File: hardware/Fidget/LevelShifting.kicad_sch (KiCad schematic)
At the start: 20 parts

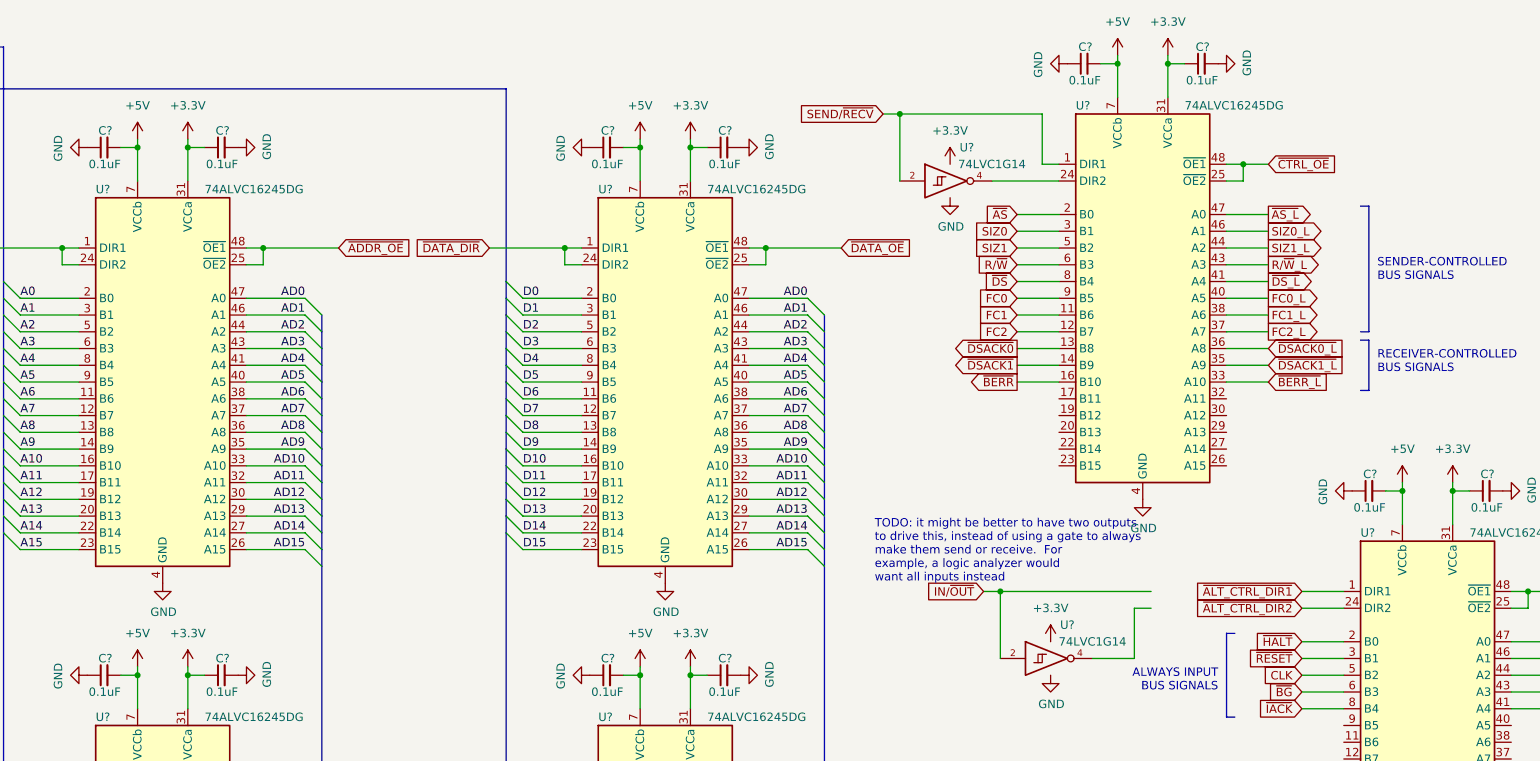
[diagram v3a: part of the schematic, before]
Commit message: Added jumper to select bus voltage
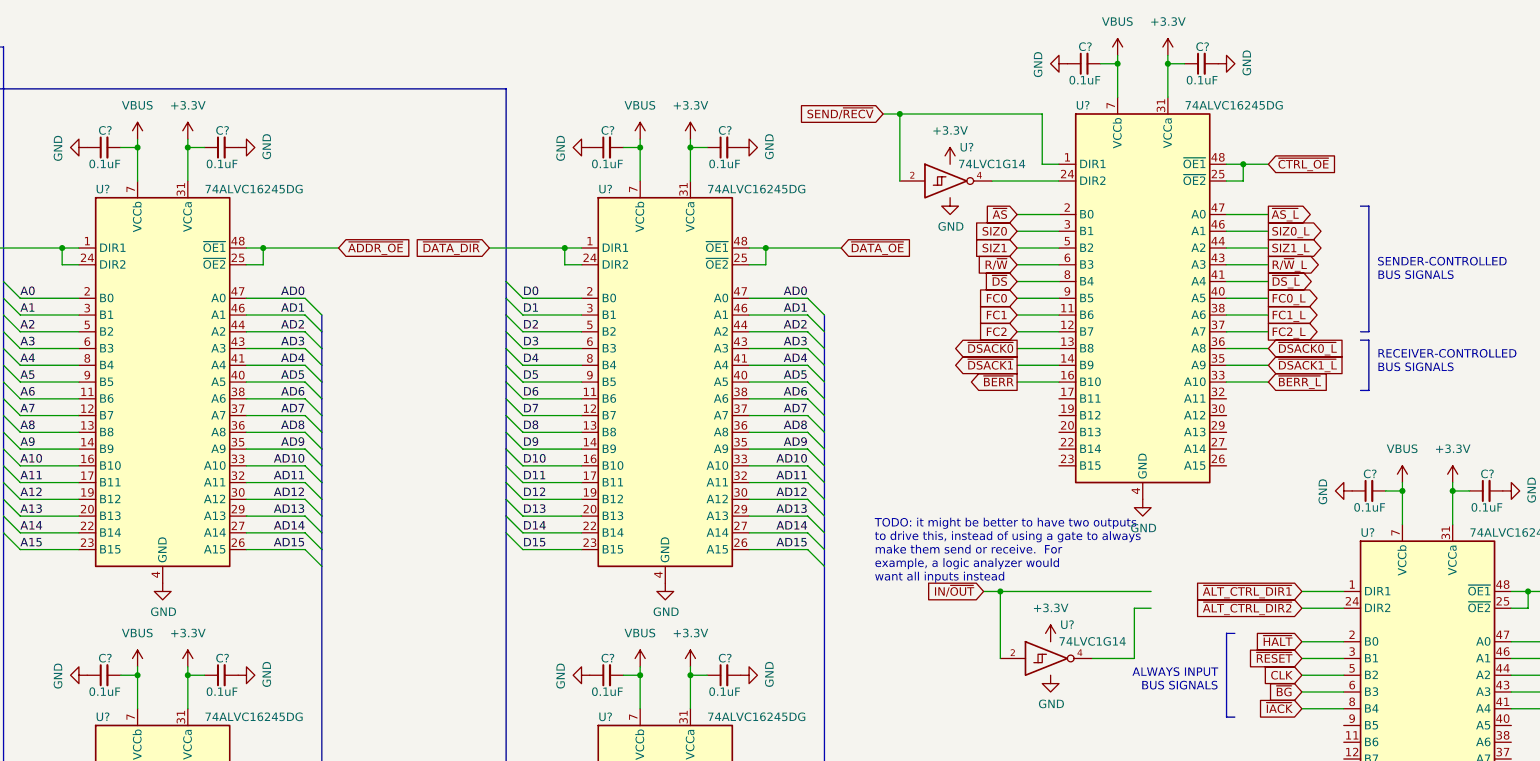
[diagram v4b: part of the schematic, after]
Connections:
- net +5V renamed VBUS
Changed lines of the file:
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@@
+    (pin "1")
+  )
+  (symbol (lib_id "power:VBUS") (at 54.61 114.3 0) (unit 1)
+    (in_bom yes) (on_board yes) (fields_autoplaced)
+    (property "Reference" "#PWR?" (id 0) (at 54.61 118.11 0)
+      (effects (font (size 1.27 1.27)) hide)
+    )
+    (property "Value" "VBUS" (id 1) (at 54.61 109.22 0))
+    (property "Footprint" "" (id 2) (at 54.61 114.3 0)
+      (effects (font (size 1.27 1.27)) hide)
+    )
+    (property "Datasheet" "" (id 3) (at 54.61 114.3 0)
+      (effects (font (size 1.27 1.27)) hide)
+    )
+    (pin "1")
+  )
+  (symbol (lib_id "power:VBUS") (at 203.2 21.59 0) (unit 1)
+    (in_bom yes) (on_board yes) (fields_autoplaced)
+    (property "Reference" "#PWR?" (id 0) (at 203.2 25.4 0)
+      (effects (font (size 1.27 1.27)) hide)
+    )
+    (property "Value" "VBUS" (id 1) (at 203.2 16.51 0))
+    (property "Footprint" "" (id 2) (at 203.2 21.59 0)
+      (effects (font (size 1.27 1.27)) hide)
+    )
+    (property "Datasheet" "" (id 3) (at 203.2 21.59 0)
+      (effects (font (size 1.27 1.27)) hide)
+    )
     (pin "1")
   )
@@
     (pin "1")
     (pin "2")
+  )
+  (symbol (lib_id "power:VBUS") (at 246.38 86.36 0) (unit 1)
+    (in_bom yes) (on_board yes) (fields_autoplaced)
+    (property "Reference" "#PWR?" (id 0) (at 246.38 90.17 0)
+      (effects (font (size 1.27 1.27)) hide)
+    )
+    (property "Value" "VBUS" (id 1) (at 246.38 81.28 0))
+    (property "Footprint" "" (id 2) (at 246.38 86.36 0)
+      (effects (font (size 1.27 1.27)) hide)
+    )
+    (property "Datasheet" "" (id 3) (at 246.38 86.36 0)
+      (effects (font (size 1.27 1.27)) hide)
+    )
+    (pin "1")
   )
   (symbol (lib_id "power:GND") (at 261.62 87.63 90) (unit 1)
@@
     (pin "1")
   )
-  (symbol (lib_id "power:+5V") (at 246.38 86.36 0) (unit 1)
-    (in_bom yes) (on_board yes) (fields_autoplaced)
-    (property "Reference" "#PWR?" (id 0) (at 246.38 90.17 0)
-      (effects (font (size 1.27 1.27)) hide)
-    )
-    (property "Value" "+5V" (id 1) (at 246.38 81.28 0))
-    (property "Footprint" "" (id 2) (at 246.38 86.36 0)
-      (effects (font (size 1.27 1.27)) hide)
-    )
-    (property "Datasheet" "" (id 3) (at 246.38 86.36 0)
-      (effects (font (size 1.27 1.27)) hide)
-    )
-    (pin "1")
-  )
   (symbol (lib_id "power:+3.3V") (at 210.82 21.59 0) (unit 1)
     (in_bom yes) (on_board yes) (fields_autoplaced)
@@
     )
     (property "Datasheet" "" (id 3) (at 254 86.36 0)
-      (effects (font (size 1.27 1.27)) hide)
-    )
-    (pin "1")
-  )
-  (symbol (lib_id "power:+5V") (at 54.61 114.3 0) (unit 1)
-    (in_bom yes) (on_board yes) (fields_autoplaced)
-    (property "Reference" "#PWR?" (id 0) (at 54.61 118.11 0)
-      (effects (font (size 1.27 1.27)) hide)
-    )
-    (property "Value" "+5V" (id 1) (at 54.61 109.22 0))
-    (property "Footprint" "" (id 2) (at 54.61 114.3 0)
-      (effects (font (size 1.27 1.27)) hide)
-    )
-    (property "Datasheet" "" (id 3) (at 54.61 114.3 0)
       (effects (font (size 1.27 1.27)) hide)
     )
@@
     (pin "5")
   )
+  (symbol (lib_id "power:VBUS") (at 130.81 114.3 0) (unit 1)
+    (in_bom yes) (on_board yes) (fields_autoplaced)
+    (property "Reference" "#PWR?" (id 0) (at 130.81 118.11 0)
+      (effects (font (size 1.27 1.27)) hide)
+    )
+    (property "Value" "VBUS" (id 1) (at 130.81 109.22 0))
+    (property "Footprint" "" (id 2) (at 130.81 114.3 0)
+      (effects (font (size 1.27 1.27)) hide)
+    )
+    (property "Datasheet" "" (id 3) (at 130.81 114.3 0)
+      (effects (font (size 1.27 1.27)) hide)
+    )
+    (pin "1")
+  )
   (symbol (lib_id "power:GND") (at 218.44 22.86 90) (unit 1)
     (in_bom yes) (on_board yes)
@@
     (pin "1")
   )
-  (symbol (lib_id "power:+5V") (at 130.81 114.3 0) (unit 1)
-    (in_bom yes) (on_board yes) (fields_autoplaced)
-    (property "Reference" "#PWR?" (id 0) (at 130.81 118.11 0)
-      (effects (font (size 1.27 1.27)) hide)
-    )
-    (property "Value" "+5V" (id 1) (at 130.81 109.22 0))
-    (property "Footprint" "" (id 2) (at 130.81 114.3 0)
-      (effects (font (size 1.27 1.27)) hide)
-    )
-    (property "Datasheet" "" (id 3) (at 130.81 114.3 0)
-      (effects (font (size 1.27 1.27)) hide)
-    )
-    (pin "1")
-  )
-  (symbol (lib_id "power:+5V") (at 54.61 34.29 0) (unit 1)
-    (in_bom yes) (on_board yes) (fields_autoplaced)
-    (property "Reference" "#PWR0136" (id 0) (at 54.61 38.1 0)
-      (effects (font (size 1.27 1.27)) hide)
-    )
-    (property "Value" "+5V" (id 1) (at 54.61 29.21 0))
-    (property "Footprint" "" (id 2) (at 54.61 34.29 0)
-      (effects (font (size 1.27 1.27)) hide)
-    )
-    (property "Datasheet" "" (id 3) (at 54.61 34.29 0)
-      (effects (font (size 1.27 1.27)) hide)
-    )
-    (pin "1")
-  )
   (symbol (lib_id "power:GND") (at 58.42 181.61 0) (unit 1)
     (in_bom yes) (on_board yes)
@@
     (pin "9")
   )
-  (symbol (lib_id "power:+5V") (at 130.81 34.29 0) (unit 1)
-    (in_bom yes) (on_board yes) (fields_autoplaced)
-    (property "Reference" "#PWR?" (id 0) (at 130.81 38.1 0)
-      (effects (font (size 1.27 1.27)) hide)
-    )
-    (property "Value" "+5V" (id 1) (at 130.81 29.21 0))
-    (property "Footprint" "" (id 2) (at 130.81 34.29 0)
-      (effects (font (size 1.27 1.27)) hide)
-    )
-    (property "Datasheet" "" (id 3) (at 130.81 34.29 0)
+  (symbol (lib_id "power:VBUS") (at 54.61 34.29 0) (unit 1)
+    (in_bom yes) (on_board yes) (fields_autoplaced)
+    (property "Reference" "#PWR?" (id 0) (at 54.61 38.1 0)
+      (effects (font (size 1.27 1.27)) hide)
+    )
+    (property "Value" "VBUS" (id 1) (at 54.61 29.21 0))
+    (property "Footprint" "" (id 2) (at 54.61 34.29 0)
+      (effects (font (size 1.27 1.27)) hide)
+    )
+    (property "Datasheet" "" (id 3) (at 54.61 34.29 0)
       (effects (font (size 1.27 1.27)) hide)
     )
@@
     (pin "9")
   )
-  (symbol (lib_id "power:+5V") (at 203.2 21.59 0) (unit 1)
-    (in_bom yes) (on_board yes) (fields_autoplaced)
-    (property "Reference" "#PWR?" (id 0) (at 203.2 25.4 0)
-      (effects (font (size 1.27 1.27)) hide)
-    )
-    (property "Value" "+5V" (id 1) (at 203.2 16.51 0))
-    (property "Footprint" "" (id 2) (at 203.2 21.59 0)
-      (effects (font (size 1.27 1.27)) hide)
-    )
-    (property "Datasheet" "" (id 3) (at 203.2 21.59 0)
-      (effects (font (size 1.27 1.27)) hide)
-    )
-    (pin "1")
-  )
   (symbol (lib_id "Device:C_Small") (at 143.51 115.57 90) (unit 1)
     (in_bom yes) (on_board yes)
@@
       (effects (font (size 1.27 1.27)) hide)
     )
+    (pin "1")
+  )
+  (symbol (lib_id "power:VBUS") (at 130.81 34.29 0) (unit 1)
+    (in_bom yes) (on_board yes) (fields_autoplaced)
+    (property "Reference" "#PWR?" (id 0) (at 130.81 38.1 0)
+      (effects (font (size 1.27 1.27)) hide)
+    )
+    (property "Value" "VBUS" (id 1) (at 130.81 29.21 0))
+    (property "Footprint" "" (id 2) (at 130.81 34.29 0)
+      (effects (font (size 1.27 1.27)) hide)
+    )
+    (property "Datasheet" "" (id 3) (at 130.81 34.29 0)
+      (effects (font (size 1.27 1.27)) hide)
+    )

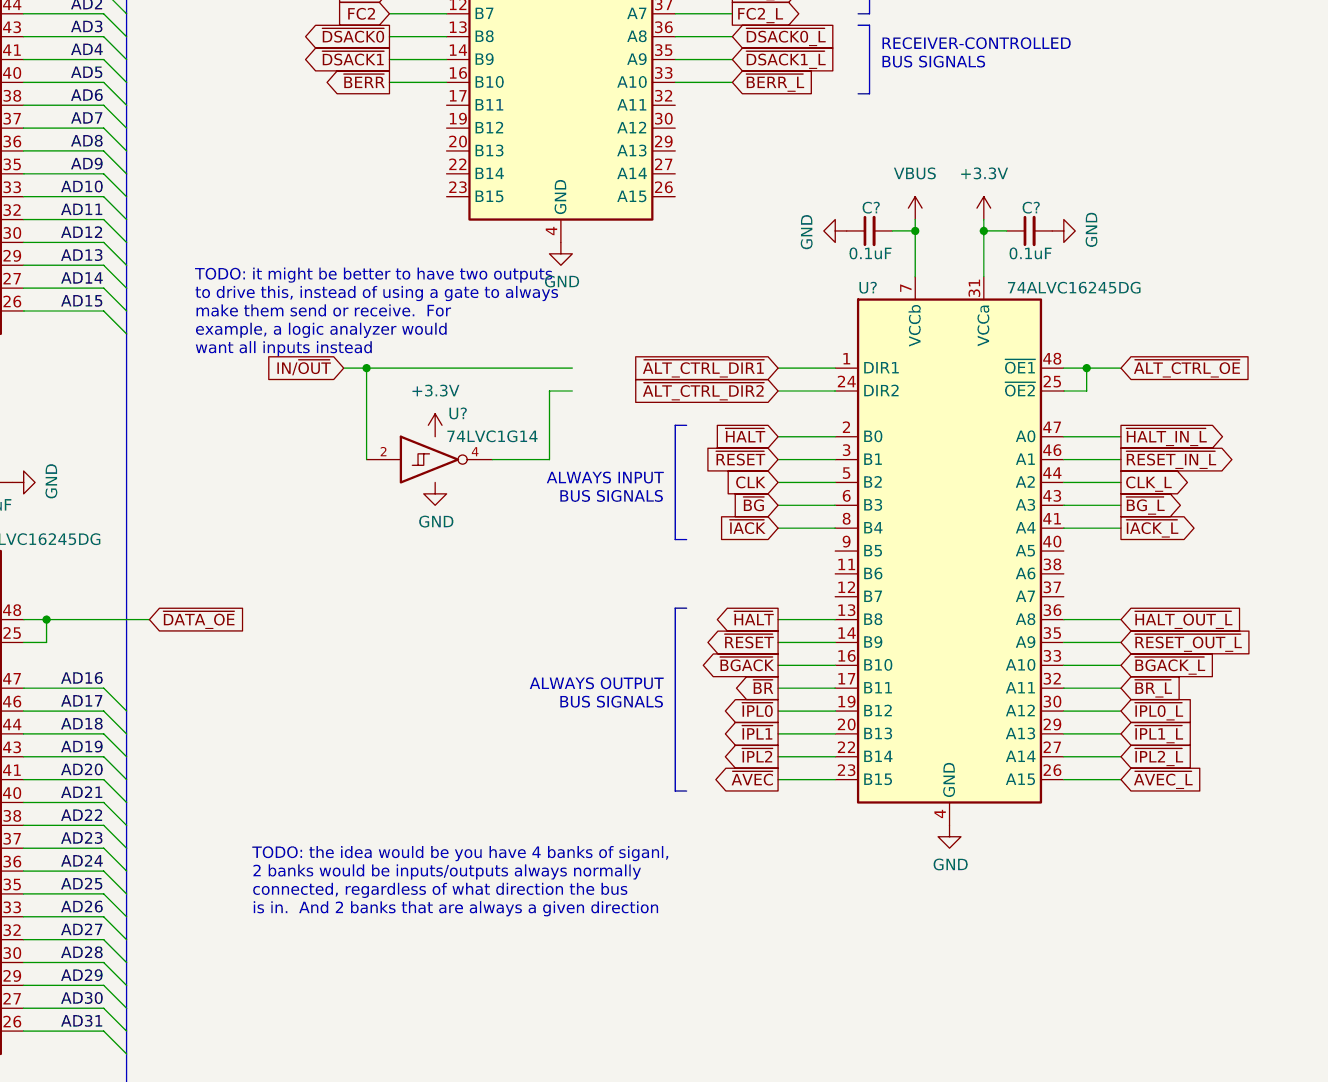
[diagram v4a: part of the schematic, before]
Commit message: Filled in more details in schematic
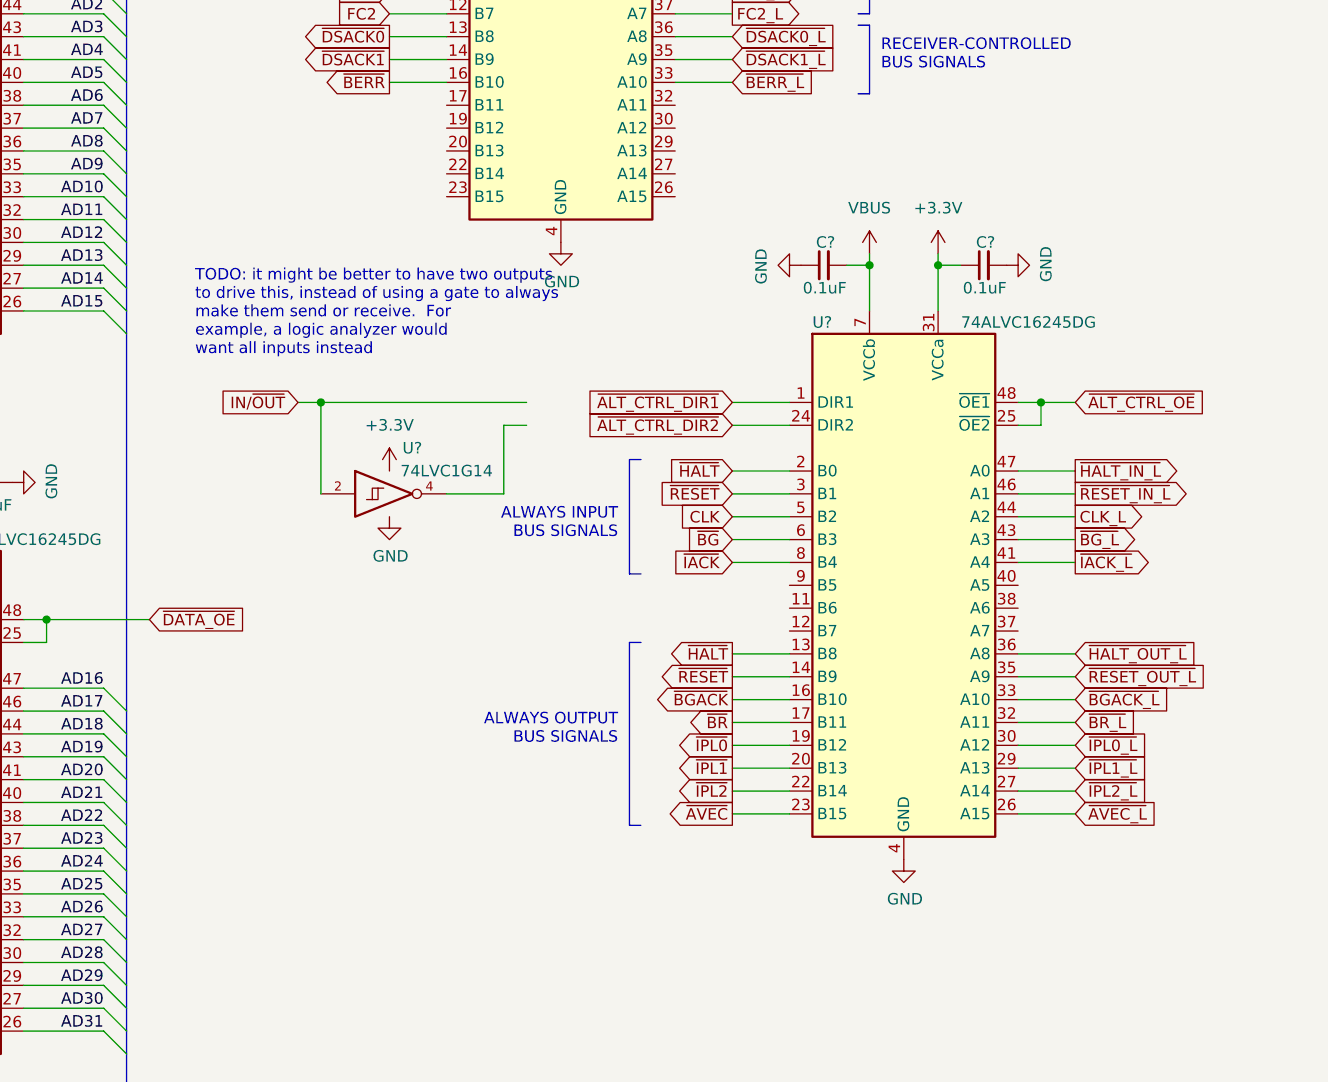
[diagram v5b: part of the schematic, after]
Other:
- note removed: "TODO: the idea would be you have 4 banks of siganl, 2 banks would be inputs/outputs always normally connected, regardless of what direction the bus is in. And 2 banks that are always a given direction"
- moved on the sheet: C?, U?
